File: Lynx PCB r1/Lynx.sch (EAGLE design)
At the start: 77 parts, among them IC1 MCP1703DB, Q1 8MHz, X1 BU-SMA-V, X2 332-02, X3 332-02

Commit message: PCB WIP
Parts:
- added C37: 0.1uF, rcl:C-EUC0603
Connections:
- removed net N$14: DAC1.I_OUT, R3.1
- removed net N$15: DAC1.!I_OUT!, R4.2
- removed net N$28: DAC2.!I_OUT!, R5.1
- removed net N$29: DAC2.I_OUT, R6.2
- new net MOD-RF: IQ_MOD.RF@11, X1.1
- net +3V3: now also C30.1, C31.1, C32.1, C33.1, C37.1
- net BBMI: now also DAC1.!I_OUT!, R4.2
- net BBMQ: now also DAC2.I_OUT, R6.2
- net BBPI: now also DAC1.I_OUT, R3.1
- net BBPQ: now also DAC2.!I_OUT!, R5.1
- net GND: now also C30.2, C31.2, C32.2, C33.2, C37.2
- net LO: no longer X1.1
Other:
- moved on the sheet: C30, C31, C32, C33, X1

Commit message: rf routing
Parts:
- removed STATUS-1, STATUS-2: BI-LED-CC, Lynx components:BI-LED-CC
- added -3V3, BBMI, BBMQ, BBPI, BBPQ, I_BUF, Q_BUF: PTR1PAD1-13Y, testpad:PTR1PAD1-13Y
- added C38, C39, C40: 150pF, rcl:C-EUC0603
- added C41, C42: 10uF, rcl:CPOL-EUSANYO_SMD_B6
- added IC2: (no value), linear:2AMP_P8+4D
- added IC3: ICL7660, maxim:ICL7660CSA
- added R10, R11, R12, R9: 1500, resistor:R-EU_R0603
- added RESET: DTSM-6, switch-tact:DTSM-6
- added S1, S2: BI-LED-CC, Lynx components:BI-LED-CC
- added U$4, U$5: AD8476, Lynx components:AD8476
- C37: value 0.1uF -> 150pF
- R3, R6: value 50 -> 100
- R4, R5: value 50 -> 1500
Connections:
- removed net MOD-RF: IQ_MOD.RF@11, X1.1
- new net +0.54V: R11.1, R12.2, U$4.VOCM, U$5.VOCM
- new net -3V3: -3V3.TP, C42.-, IC2P.V-, IC3.VOUT, U$4.-VS, U$5.-VS
- new net GND1: IC2A.-IN, IC2A.OUT, I_BUF.TP, R4.1
- new net GND2: IC2B.-IN, IC2B.OUT, Q_BUF.TP, R5.1
- new net N$14: DAC1.I_OUT, IC2A.+IN, R3.1
- new net N$29: DAC2.I_OUT, IC2B.+IN, R6.2
- new net N$31: C37.2, R4.2, R9.1
- new net N$32: C38.2, R9.2, U$4.INP
- new net N$34: C41.-, IC3.CAP-
- new net N$35: C39.2, R10.1, R5.2
- new net N$36: C40.2, R10.2, U$5.INP
- new net N$37: C41.+, IC3.CAP+
- net +3V3: now also IC2P.V+, IC3.V+, R11.2, U$4.+VS, U$5.+VS; no longer C37.1
- net BBMI: now also BBMI.TP, U$4.-OUT; no longer DAC1.!I_OUT!, R4.2
- net BBMQ: now also BBMQ.TP, U$5.-OUT; no longer DAC2.I_OUT, R6.2
- net BBPI: now also BBPI.TP, U$4.+OUT; no longer DAC1.I_OUT, R3.1
- net BBPQ: now also BBPQ.TP, U$5.+OUT; no longer DAC2.!I_OUT!, R5.1
- net GND: now also C37.1, C38.1, C39.1, C40.1, C42.+, DAC1.!I_OUT!, DAC2.!I_OUT!, IC3.GND, IC3.LV, R12.1, RESET.3, RESET.4, S1.P$1, S2.P$1, U$4.INN, U$5.INN; no longer C37.2, R4.1, R5.2, STATUS-1.P$1, STATUS-2.P$1
- net LO: now also X1.1
- net N$16: now also S1.P$2; no longer STATUS-1.P$2
- net N$17: now also S1.P$3; no longer STATUS-1.P$3
- net N$18: now also S2.P$2; no longer STATUS-2.P$2
- net N$19: now also S2.P$3; no longer STATUS-2.P$3
- net NRST: now also RESET.1, RESET.2
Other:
- note removed: "Some low pass magic"
- moved on the sheet: 10MHZ, 3V3, 5V_IN, C1, C10, C11, C12, C13, C14, C15, C16, C17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

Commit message: Power supply and jumpers
So many jumpers
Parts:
- removed IC1: MCP1703DB, linear:MCP1703DB
- removed X2, X3: 332-02, con-garry:332-02
- added 3V3-REG, 5V-REG: MCP1703DB, linear:MCP1703DB
- added C43, C44: 0.1uF, rcl:C-EUC0603
- added JP1, JP2, JP3, JP4, JP5, JP6, JP7, JP8, JP9: (no value), pinhead:PINHD-1X2
- renumbered U$2 to SWD-HEADER
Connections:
- removed net BATTERY-OUT: C36.1, IC1.VI, X2-1.S
- removed net DAC_SLEEP: DAC1.SLEEP, DAC2.SLEEP
- removed net N$43: X2-2.S, X3-1.S
- new net DAC-SLEEP: DAC1.SLEEP, DAC2.SLEEP, U$1PORT_A.PA11
- new net N$15: JP6.2, U$5.-OUT
- new net N$28: JP7.1, U$5.+OUT
- new net N$38: 3V3-REG.VO, C35.1, JP1.1
- new net N$39: 5V-REG.VO, C43.1, JP2.1
- new net N$40: JP8.2, U$4.+OUT
- new net N$41: JP9.1, U$4.-OUT
- new net POWER-IN: 3V3-REG.VI, 5V-REG.VI, C36.1, C44.1, JP5.2
- net +3V3: now also JP1.2, JP3.2; no longer C35.1, IC1.VO
- net +5V: now also JP2.2, JP4.2
- net BBMI: now also JP8.1; no longer U$4.-OUT
- net BBMQ: now also JP6.1; no longer U$5.-OUT
- net BBPI: now also JP9.2; no longer U$4.+OUT
- net BBPQ: now also JP7.2; no longer U$5.+OUT
- net DAC-CLK: now also U$1PORT_A.PA12
- net GND: now also 3V3-REG.GND, 5V-REG.GND, C43.2, C44.2, JP3.1, JP4.1, JP5.1; no longer IC1.GND, X3-2.S
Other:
- note added: "Alternate power supply in"
- note added: "supply socket"
- moved on the sheet: -3V3, C35, C36, C41, C42, IC3

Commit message: Complete rf reroute
Shuffled a 'lot' of things around. Ripped up everything past the op-amps
and made it a lot nicer.
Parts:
- removed 3V3, 5V_IN, BBMI, BBMQ, BBPI, BBPQ: PTR1PAD1-13Y, testpad:PTR1PAD1-13Y
- removed C28: 1uF, rcl:C-EUC0603
- removed R11, R12: 1500, resistor:R-EU_R0603
- added BOOT0: DTSM-6, switch-tact:DTSM-6
- added C45: 0.1uF, rcl:C-EUC0603
- added JP10: Power In, pinhead:PINHD-1X2
- added R13: 1500, resistor:R-EU_R0603
- added X2: BU-SMA-V, con-coax:BU-SMA-V
- 3V3-REG, 5V-REG: value MCP1703DB -> V-REG; device linear:MCP1703DB -> Lynx components:VOLTAGE-REGULATOR
- C35, C36, C43, C44: value 0.1uF -> 1uF
- JP1: value (none) -> 3v3 reg
- JP2: value (none) -> 5v reg
- JP3: value (none) -> 3v3 in
- JP4: value (none) -> 5v in
- JP5: value (none) -> Power In
- JP6: value (none) -> BBMQ
- JP7: value (none) -> BBPQ
- JP8: value (none) -> BBMI
- JP9: value (none) -> BBPI
- R8: device rcl:R-EU_R0805 -> rcl:R-EU_R0603
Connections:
- net GND1 renamed I_BUF
- net GND2 renamed Q_BUF
- removed net N$41: JP9.1, U$4.-OUT
- removed net PLL_MUTE: U$3.!MUTE!
- new net 5V-REG: 5V-REG.VO, 5V-REG.VO@1, C43.1, JP2.1
- new net N$30: R8.1, U$3.V_VCO+
- new net RF-MOD: IQ_MOD.RF@11, X2.1
- net +0.54V: no longer R11.1, R12.2
- net +3V3: now also BOOT0.1, BOOT0.2, U$3.!MUTE!; no longer 3V3.TP, R11.2
- net +5V: no longer 5V_IN.TP, C28.2, R8.1, U$3.V_VCO+
- net BBMI: no longer BBMI.TP
- net BBMQ: no longer BBMQ.TP
- net BBPI: no longer BBPI.TP
- net BBPQ: no longer BBPQ.TP
- net BOOT0: now also BOOT0.3, BOOT0.4, R13.2
- net GND: now also C45.1, JP10.1, R13.1, X2.2; no longer C28.1, R12.1
- net N$15: now also U$4.+OUT; no longer U$5.-OUT
- net N$28: now also U$4.-OUT; no longer U$5.+OUT
- net N$38: now also 3V3-REG.VO@1
- net N$39: now also JP8.2, U$5.-OUT; no longer 5V-REG.VO, C43.1, JP2.1
- net N$40: now also JP9.1, U$5.+OUT; no longer JP8.2, U$4.+OUT
- net NRST: now also C45.2
- net POWER-IN: now also JP10.2
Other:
- moved on the sheet: 10MHZ, C1, C29, C30, C31, C32, C33, C34, C4, C5, C6, C7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

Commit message: All routed
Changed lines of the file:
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@@
 <setting verticaltext="up"/>
 </settings>
-<grid distance="0.05" unitdist="inch" unit="inch" style="lines" multiple="1" display="no" altdistance="0.01" altunitdist="inch" altunit="inch"/>
+<grid distance="0.1" unitdist="inch" unit="inch" style="lines" multiple="1" display="no" altdistance="0.01" altunitdist="inch" altunit="inch"/>
 <layers>
-<layer number="1" name="Top" color="4" fill="1" visible="yes" active="no"/>
-<layer number="2" name="Route2" color="1" fill="3" visible="yes" active="no"/>
-<layer number="3" name="Route3" color="4" fill="3" visible="yes" active="no"/>
-<layer number="4" name="Route4" color="1" fill="4" visible="yes" active="no"/>
-<layer number="5" name="Route5" color="4" fill="4" visible="yes" active="no"/>
-<layer number="6" name="Route6" color="1" fill="8" visible="yes" active="no"/>
-<layer number="7" name="Route7" color="4" fill="8" visible="yes" active="no"/>
-<layer number="8" name="Route8" color="1" fill="2" visible="yes" active="no"/>
-<layer number="9" name="Route9" color="4" fill="2" visible="yes" active="no"/>
-<layer number="10" name="Route10" color="1" fill="7" visible="yes" active="no"/>
-<layer number="11" name="Route11" color="4" fill="7" visible="yes" active="no"/>
-<layer number="12" name="Route12" color="1" fill="5" visible="yes" active="no"/>
-<layer number="13" name="Route13" color="4" fill="5" visible="yes" active="no"/>
-<layer number="14" name="Route14" color="1" fill="6" visible="yes" active="no"/>
-<layer number="15" name="Route15" color="4" fill="6" visible="yes" active="no"/>
-<layer number="16" name="Bottom" color="1" fill="1" visible="yes" active="no"/>
-<layer number="17" name="Pads" color="2" fill="1" visible="yes" active="no"/>
-<layer number="18" name="Vias" color="2" fill="1" visible="yes" active="no"/>
-<layer number="19" name="Unrouted" color="6" fill="1" visible="yes" active="no"/>
-<layer number="20" name="Dimension" color="15" fill="1" visible="yes" active="no"/>
-<layer number="21" name="tPlace" color="7" fill="1" visible="yes" active="no"/>
-<layer number="22" name="bPlace" color="7" fill="1" visible="yes" active="no"/>
-<layer number="23" name="tOrigins" color="15" fill="1" visible="yes" active="no"/>
-<layer number="24" name="bOrigins" color="15" fill="1" visible="yes" active="no"/>
-<layer number="25" name="tNames" color="7" fill="1" visible="yes" active="no"/>
-<layer number="26" name="bNames" color="7" fill="1" visible="yes" active="no"/>
-<layer number="27" name="tValues" color="7" fill="1" visible="yes" active="no"/>
-<layer number="28" name="bValues" color="7" fill="1" visible="yes" active="no"/>
+<layer number="1" name="Top" color="4" fill="1" visible="no" active="no"/>
+<layer number="2" name="Route2" color="1" fill="3" visible="no" active="no"/>
+<layer number="3" name="Route3" color="4" fill="3" visible="no" active="no"/>
+<layer number="4" name="Route4" color="1" fill="4" visible="no" active="no"/>
+<layer number="5" name="Route5" color="4" fill="4" visible="no" active="no"/>
+<layer number="6" name="Route6" color="1" fill="8" visible="no" active="no"/>
+<layer number="7" name="Route7" color="4" fill="8" visible="no" active="no"/>
+<layer number="8" name="Route8" color="1" fill="2" visible="no" active="no"/>
+<layer number="9" name="Route9" color="4" fill="2" visible="no" active="no"/>
+<layer number="10" name="Route10" color="1" fill="7" visible="no" active="no"/>
+<layer number="11" name="Route11" color="4" fill="7" visible="no" active="no"/>
+<layer number="12" name="Route12" color="1" fill="5" visible="no" active="no"/>
+<layer number="13" name="Route13" color="4" fill="5" visible="no" active="no"/>
+<layer number="14" name="Route14" color="1" fill="6" visible="no" active="no"/>
+<layer number="15" name="Route15" color="4" fill="6" visible="no" active="no"/>
+<layer number="16" name="Bottom" color="1" fill="1" visible="no" active="no"/>
+<layer number="17" name="Pads" color="2" fill="1" visible="no" active="no"/>
+<layer number="18" name="Vias" color="2" fill="1" visible="no" active="no"/>
+<layer number="19" name="Unrouted" color="6" fill="1" visible="no" active="no"/>
+<layer number="20" name="Dimension" color="15" fill="1" visible="no" active="no"/>
+<layer number="21" name="tPlace" color="7" fill="1" visible="no" active="no"/>
+<layer number="22" name="bPlace" color="7" fill="1" visible="no" active="no"/>
+<layer number="23" name="tOrigins" color="15" fill="1" visible="no" active="no"/>
+<layer number="24" name="bOrigins" color="15" fill="1" visible="no" active="no"/>
+<layer number="25" name="tNames" color="7" fill="1" visible="no" active="no"/>
+<layer number="26" name="bNames" color="7" fill="1" visible="no" active="no"/>
+<layer number="27" name="tValues" color="7" fill="1" visible="no" active="no"/>
+<layer number="28" name="bValues" color="7" fill="1" visible="no" active="no"/>
 <layer number="29" name="tStop" color="7" fill="3" visible="no" active="no"/>
 <layer number="30" name="bStop" color="7" fill="6" visible="no" active="no"/>
@@
 <layer number="35" name="tGlue" color="7" fill="4" visible="no" active="no"/>
 <layer number="36" name="bGlue" color="7" fill="5" visible="no" active="no"/>
-<layer number="37" name="tTest" color="7" fill="1" visible="yes" active="no"/>
-<layer number="38" name="bTest" color="7" fill="1" visible="yes" active="no"/>
+<layer number="37" name="tTest" color="7" fill="1" visible="no" active="no"/>
+<layer number="38" name="bTest" color="7" fill="1" visible="no" active="no"/>
 <layer number="39" name="tKeepout" color="4" fill="11" visible="no" active="no"/>
 <layer number="40" name="bKeepout" color="1" fill="11" visible="no" active="no"/>
@@
 <layer number="44" name="Drills" color="7" fill="1" visible="no" active="no"/>
 <layer number="45" name="Holes" color="7" fill="1" visible="no" active="no"/>
-<layer number="46" name="Milling" color="3" fill="1" visible="yes" active="no"/>
-<layer number="47" name="Measures" color="7" fill="1" visible="yes" active="no"/>
-<layer number="48" name="Document" color="7" fill="1" visible="yes" active="no"/>
-<layer number="49" name="Reference" color="7" fill="1" visible="yes" active="no"/>
-<layer number="50" name="dxf" color="7" fill="1" visible="yes" active="no"/>
-<layer number="51" name="tDocu" color="7" fill="1" visible="yes" active="no"/>
-<layer number="52" name="bDocu" color="7" fill="1" visible="yes" active="no"/>
-<layer number="53" name="tGND_GNDA" color="7" fill="9" visible="yes" active="no"/>
-<layer number="54" name="bGND_GNDA" color="1" fill="9" visible="yes" active="no"/>
-<layer number="56" name="wert" color="7" fill="1" visible="yes" active="no"/>
+<layer number="46" name="Milling" color="3" fill="1" visible="no" active="no"/>
+<layer number="47" name="Measures" color="7" fill="1" visible="no" active="no"/>
+<layer number="48" name="Document" color="7" fill="1" visible="no" active="no"/>
+<layer number="49" name="Reference" color="7" fill="1" visible="no" active="no"/>
+<layer number="50" name="dxf" color="7" fill="1" visible="no" active="no"/>
+<layer number="51" name="tDocu" color="7" fill="1" visible="no" active="no"/>
+<layer number="52" name="bDocu" color="7" fill="1" visible="no" active="no"/>
+<layer number="53" name="tGND_GNDA" color="7" fill="9" visible="no" active="no"/>
+<layer number="54" name="bGND_GNDA" color="1" fill="9" visible="no" active="no"/>
+<layer number="56" name="wert" color="7" fill="1" visible="no" active="no"/>
 <layer number="91" name="Nets" color="2" fill="1" visible="yes" active="yes"/>
 <layer number="92" name="Busses" color="1" fill="1" visible="yes" active="yes"/>
@@
 <instance part="IC2" gate="A" x="-2.54" y="7.62" rot="MR180"/>
 <instance part="IC2" gate="B" x="-2.54" y="-66.04"/>
-<instance part="IC2" gate="P" x="77.47" y="-43.18"/>
+<instance part="IC2" gate="P" x="1.27" y="-30.48"/>
 <instance part="R4" gate="G$1" x="24.13" y="7.62"/>
 <instance part="R9" gate="G$1" x="39.37" y="7.62"/>
@@
 <segment>
 <pinref part="IC2" gate="P" pin="V+"/>
-<wire x1="77.47" y1="-35.56" x2="77.47" y2="-33.02" width="0.1524" layer="91"/>
-<label x="74.93" y="-33.02" size="1.778" layer="95"/>
+<wire x1="1.27" y1="-22.86" x2="1.27" y2="-20.32" width="0.1524" layer="91"/>
+<label x="-1.27" y="-20.32" size="1.778" layer="95"/>
 </segment>
 <segment>
@@
 <segment>
 <pinref part="IC2" gate="P" pin="V-"/>
-<wire x1="77.47" y1="-50.8" x2="77.47" y2="-54.61" width="0.1524" layer="91"/>
-<label x="80.01" y="-54.61" size="1.778" layer="95" rot="R180"/>
-</segment>
-<segment>
+<wire x1="1.27" y1="-38.1" x2="1.27" y2="-41.91" width="0.1524" layer="91"/>
+<label x="3.81" y="-41.91" size="1.778" layer="95" rot="R180"/>
+</segment>
+<segment>

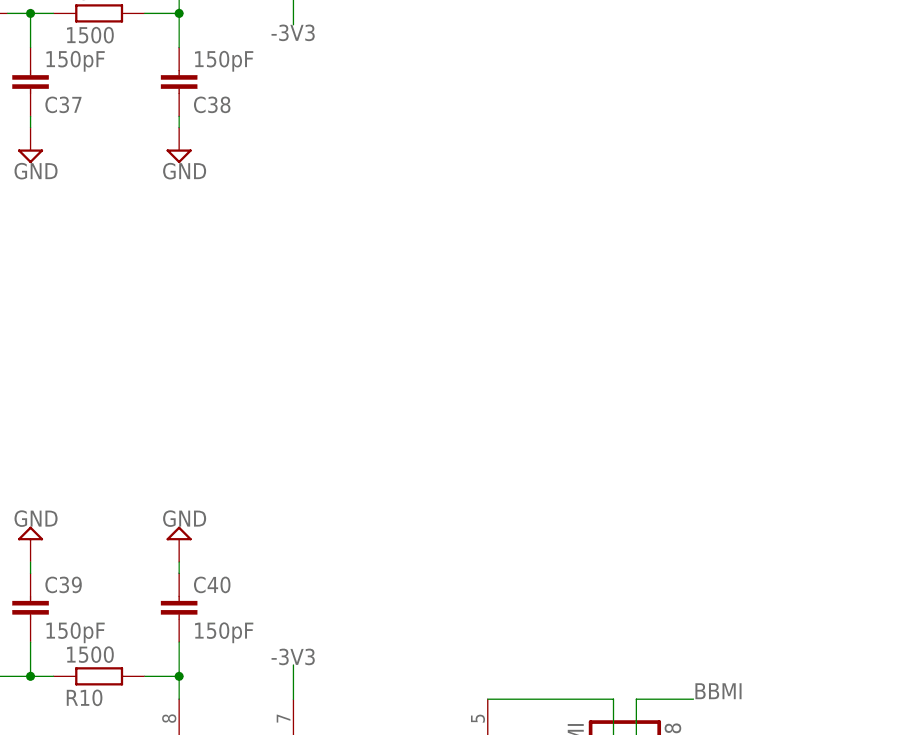
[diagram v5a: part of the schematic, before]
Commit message: Added 0.54v reference souce, made DRC happy
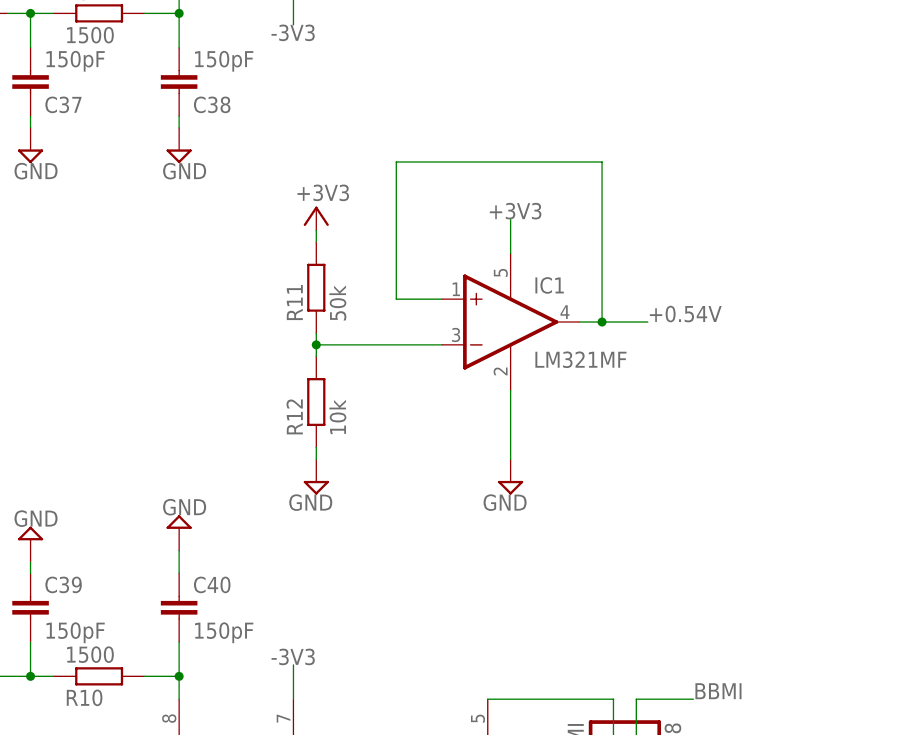
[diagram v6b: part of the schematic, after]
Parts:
- added IC1: LM321MF, linear:LM321MF
- added R11: 50k, resistor:R-EU_R0603
- added R12: 10k, resistor:R-EU_R0603
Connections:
- new net N$42: IC1.-IN, R11.1, R12.2
- net +0.54V: now also IC1.+IN, IC1.OUT
- net +3V3: now also IC1.V+, R11.2
- net GND: now also IC1.V-, R12.1
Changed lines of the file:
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@@
 <setting verticaltext="up"/>
 </settings>
-<grid distance="0.1" unitdist="inch" unit="inch" style="lines" multiple="1" display="no" altdistance="0.01" altunitdist="inch" altunit="inch"/>
+<grid distance="0.05" unitdist="inch" unit="inch" style="lines" multiple="1" display="no" altdistance="0.01" altunitdist="inch" altunit="inch"/>
 <layers>
 <layer number="1" name="Top" color="4" fill="1" visible="no" active="no"/>
@@
 <part name="+3V1" library="supply1" deviceset="+3V3" device=""/>
 <part name="JP10" library="pinhead" deviceset="PINHD-1X2" device="" value="Power In"/>
+<part name="IC1" library="linear" deviceset="LM321?*" device="MF"/>
+<part name="R11" library="resistor" deviceset="R-EU_" device="R0603" value="50k"/>
+<part name="R12" library="resistor" deviceset="R-EU_" device="R0603" value="10k"/>
+<part name="+3V17" library="supply1" deviceset="+3V3" device=""/>
+<part name="SUPPLY58" library="supply2" deviceset="GND" device=""/>
+<part name="SUPPLY59" library="supply2" deviceset="GND" device=""/>
 </parts>
 <sheets>
@@
 <instance part="C40" gate="G$1" x="48.26" y="-57.15"/>
 <instance part="SUPPLY46" gate="GND" x="31.75" y="-50.8" rot="MR180"/>
-<instance part="SUPPLY47" gate="GND" x="48.26" y="-50.8" rot="MR180"/>
+<instance part="SUPPLY47" gate="GND" x="48.26" y="-49.53" rot="MR180"/>
 <instance part="SUPPLY48" gate="GND" x="48.26" y="58.42" rot="R180"/>
 <instance part="SUPPLY49" gate="GND" x="48.26" y="-116.84"/>
@@
 <instance part="+3V1" gate="G$1" x="2.54" y="134.62" rot="R90"/>
 <instance part="JP10" gate="G$1" x="-245.11" y="-154.94" rot="R180"/>
+<instance part="IC1" gate="G$1" x="85.09" y="-26.67"/>
+<instance part="R11" gate="G$1" x="63.5" y="-22.86" rot="R90"/>
+<instance part="R12" gate="G$1" x="63.5" y="-35.56" rot="R90"/>
+<instance part="+3V17" gate="G$1" x="63.5" y="-13.97" smashed="yes">
+<attribute name="VALUE" x="67.31" y="-11.43" size="1.778" layer="96" rot="R180"/>
+</instance>
+<instance part="SUPPLY58" gate="GND" x="63.5" y="-44.45" rot="MR0"/>
+<instance part="SUPPLY59" gate="GND" x="85.09" y="-44.45" rot="MR0"/>
 </instances>
 <busses>
@@
 <pinref part="C40" gate="G$1" pin="1"/>
 <pinref part="SUPPLY47" gate="GND" pin="GND"/>
-<wire x1="48.26" y1="-54.61" x2="48.26" y2="-53.34" width="0.1524" layer="91"/>
+<wire x1="48.26" y1="-54.61" x2="48.26" y2="-52.07" width="0.1524" layer="91"/>
 </segment>
 <segment>
@@
 <wire x1="-242.57" y1="-157.48" x2="-232.41" y2="-157.48" width="0.1524" layer="91"/>
 <label x="-232.41" y="-157.48" size="1.778" layer="95"/>
+</segment>
+<segment>
+<pinref part="SUPPLY58" gate="GND" pin="GND"/>
+<pinref part="R12" gate="G$1" pin="1"/>
+<wire x1="63.5" y1="-41.91" x2="63.5" y2="-40.64" width="0.1524" layer="91"/>
+</segment>
+<segment>
+<pinref part="IC1" gate="G$1" pin="V-"/>
+<pinref part="SUPPLY59" gate="GND" pin="GND"/>
+<wire x1="85.09" y1="-41.91" x2="85.09" y2="-34.29" width="0.1524" layer="91"/>
 </segment>
 </net>
@@
 <wire x1="1.27" y1="-22.86" x2="1.27" y2="-20.32" width="0.1524" layer="91"/>
 <label x="-1.27" y="-20.32" size="1.778" layer="95"/>
+<wire x1="85.09" y1="-19.05" x2="85.09" y2="-15.24" width="0.1524" layer="91"/>
+<pinref part="IC1" gate="G$1" pin="V+"/>
+<label x="82.55" y="-15.24" size="1.778" layer="95"/>
 </segment>
 <segment>
@@
 <pinref part="+3V1" gate="G$1" pin="+3V3"/>
 </segment>
+<segment>
+<pinref part="R11" gate="G$1" pin="2"/>
+<pinref part="+3V17" gate="G$1" pin="+3V3"/>
+<wire x1="63.5" y1="-16.51" x2="63.5" y2="-17.78" width="0.1524" layer="91"/>
+</segment>
 </net>
 <net name="+5V" class="0">
@@
 <pinref part="U$5" gate="G$1" pin="VOCM"/>
 </segment>
+<segment>
+<pinref part="IC1" gate="G$1" pin="+IN"/>
+<wire x1="77.47" y1="-24.13" x2="72.39" y2="-24.13" width="0.1524" layer="91"/>
+<wire x1="72.39" y1="-24.13" x2="72.39" y2="-8.89" width="0.1524" layer="91"/>
+<wire x1="72.39" y1="-8.89" x2="95.25" y2="-8.89" width="0.1524" layer="91"/>
+<wire x1="95.25" y1="-8.89" x2="95.25" y2="-26.67" width="0.1524" layer="91"/>
+<pinref part="IC1" gate="G$1" pin="OUT"/>
+<wire x1="95.25" y1="-26.67" x2="92.71" y2="-26.67" width="0.1524" layer="91"/>
+<wire x1="95.25" y1="-26.67" x2="100.33" y2="-26.67" width="0.1524" layer="91"/>
+<junction x="95.25" y="-26.67"/>
+<label x="100.33" y="-26.67" size="1.778" layer="95"/>
+</segment>
 </net>
 <net name="-3V3" class="0">
@@
 </segment>
 </net>
+<net name="N$42" class="0">
+<segment>
+<pinref part="IC1" gate="G$1" pin="-IN"/>
+<wire x1="77.47" y1="-29.21" x2="63.5" y2="-29.21" width="0.1524" layer="91"/>
+<pinref part="R11" gate="G$1" pin="1"/>
+<wire x1="63.5" y1="-29.21" x2="63.5" y2="-27.94" width="0.1524" layer="91"/>
+<pinref part="R12" gate="G$1" pin="2"/>
+<wire x1="63.5" y1="-30.48" x2="63.5" y2="-29.21" width="0.1524" layer="91"/>
+<junction x="63.5" y="-29.21"/>
+</segment>
+</net>
